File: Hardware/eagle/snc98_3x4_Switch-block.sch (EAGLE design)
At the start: 67 parts

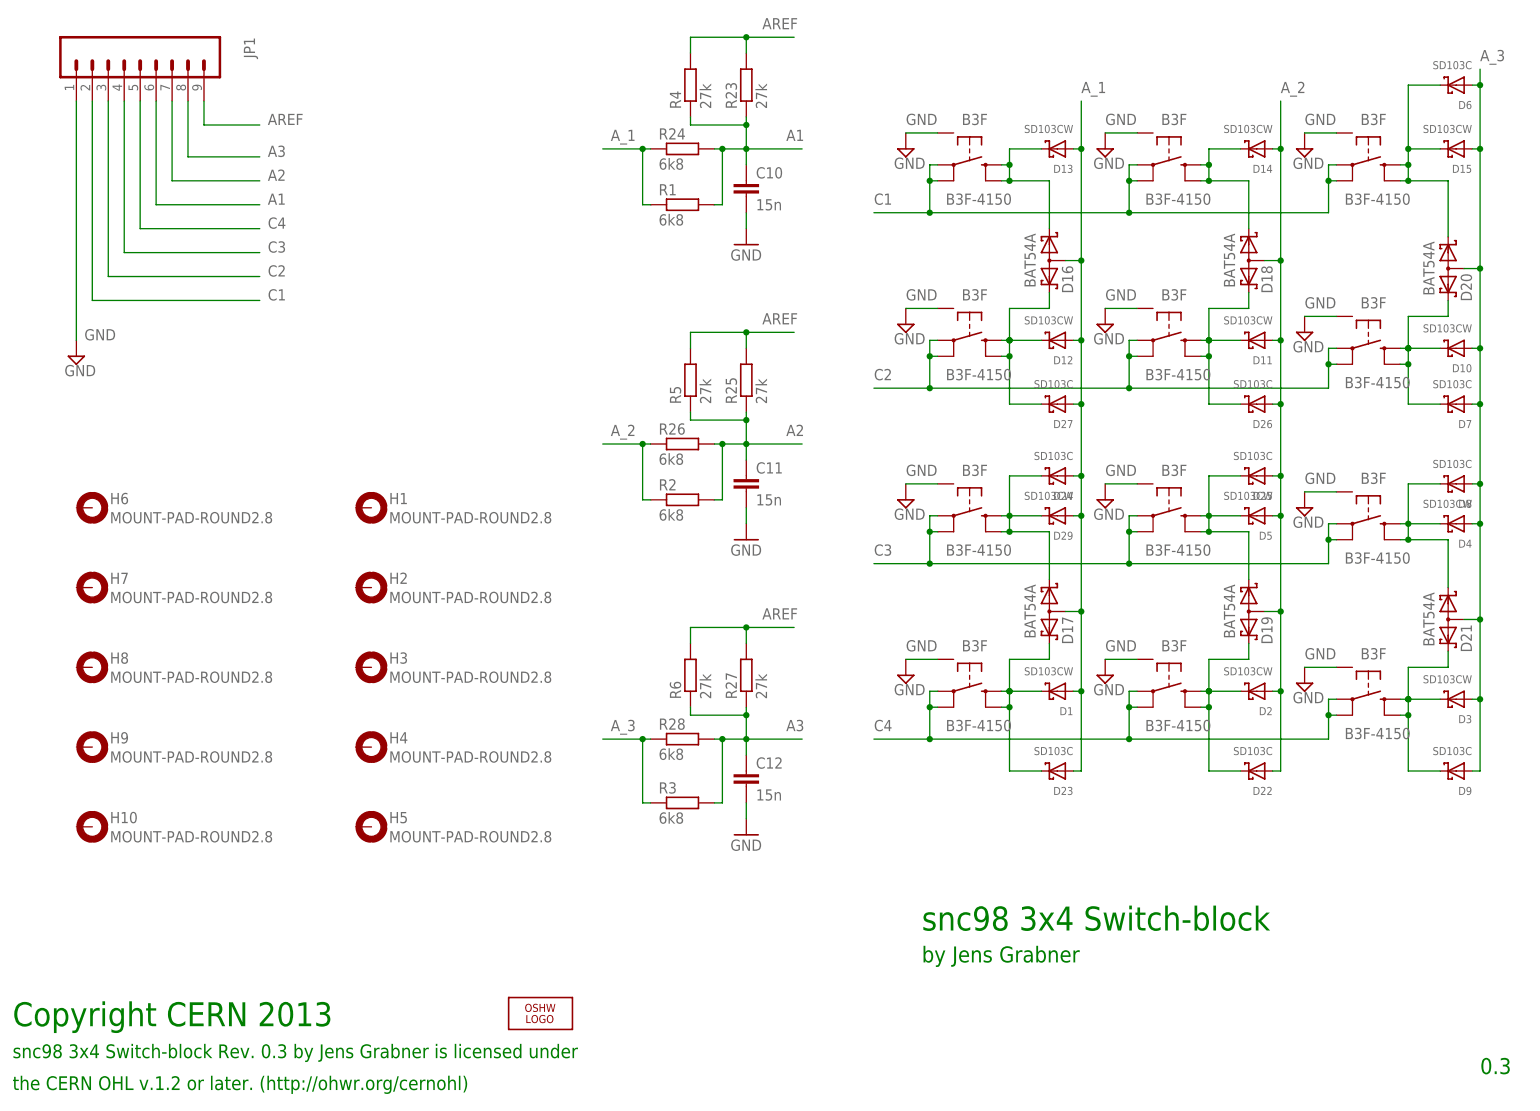
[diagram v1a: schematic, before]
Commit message: PCB cleaning V1.1
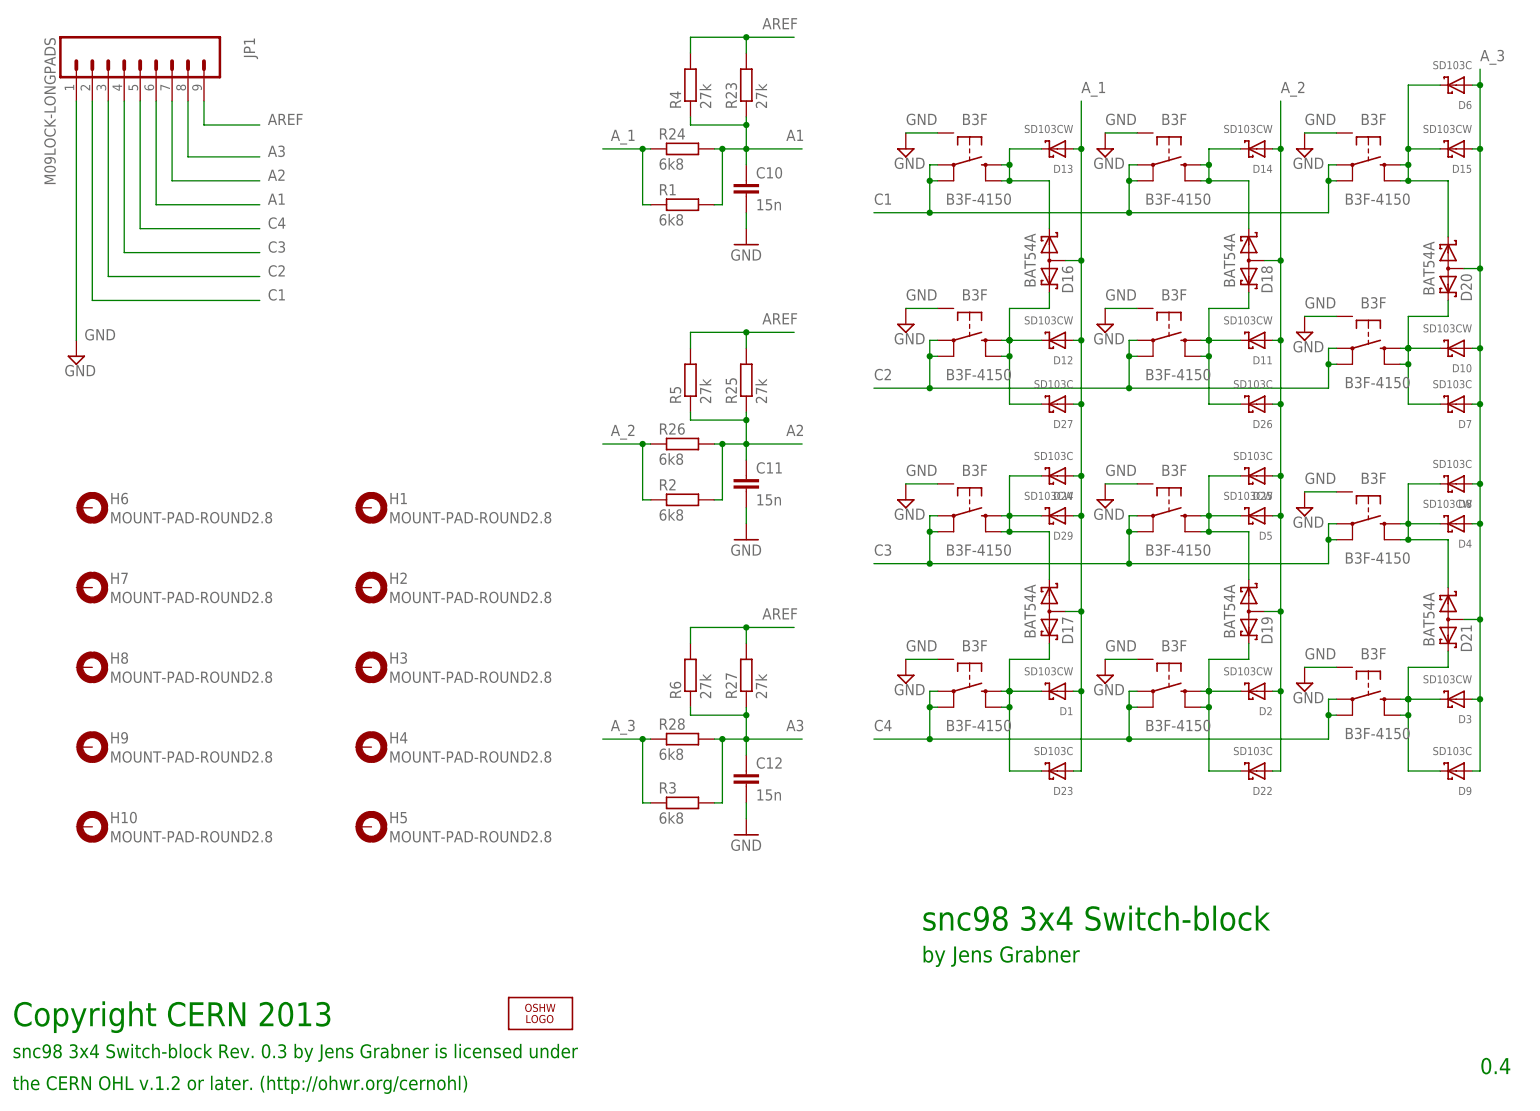
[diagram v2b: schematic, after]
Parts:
- JP1: value (none) -> M09LOCK-LONGPADS
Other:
- note added: "0.4"
- note removed: "0.3"
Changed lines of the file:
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@@
 <text x="149.86" y="30.48" size="3.81" layer="91" ratio="12">snc98 3x4 Switch-block</text>
 <text x="149.86" y="25.4" size="2.54" layer="91" ratio="12">by Jens Grabner</text>
-<text x="238.76" y="7.62" size="2.54" layer="91" ratio="12">0.3</text>
+<text x="238.76" y="7.62" size="2.54" layer="91" ratio="12">0.4</text>
 <text x="5.08" y="10.16" size="2.1844" layer="91" ratio="10">snc98 3x4 Switch-block Rev. 0.3 by Jens Grabner is licensed under</text>
 <text x="5.08" y="15.24" size="3.81" layer="91" ratio="12">Copyright CERN 2013</text>

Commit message: sinh()_cosh()_tanh() added
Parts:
- C10, C11, C12, D16, D17, D18, D19, D20, D21, H1, H4, H5, H6, H7, H8, JP1, LOGO1, R1, R2, R23, R24, R25, R26, R27, R28, R3, R4, R5, R6, S1, S10, S11, S12, S2, S3, S4, S5, S6, S7, S8, S9: OC_FARNELL (none) -> unknown
- D1, D10, D11, D12, D13, D14, D15, D2, D22, D23, D24, D25, D26, D27, D29, D3, D4, D5, D6, D7, D8, D9: MF (none) -> MULTICOMP; MPN (none) -> SD103CW-7-F; OC_FARNELL (none) -> 2306221
- H10, H2, H3, H9: value MOUNT-PAD-ROUND2.8 -> MOUNT-PAD-ROUND2.3; device holes:MOUNT-PAD-ROUND2.8 -> holes:MOUNT-PAD-ROUND2.3; OC_FARNELL (none) -> unknown

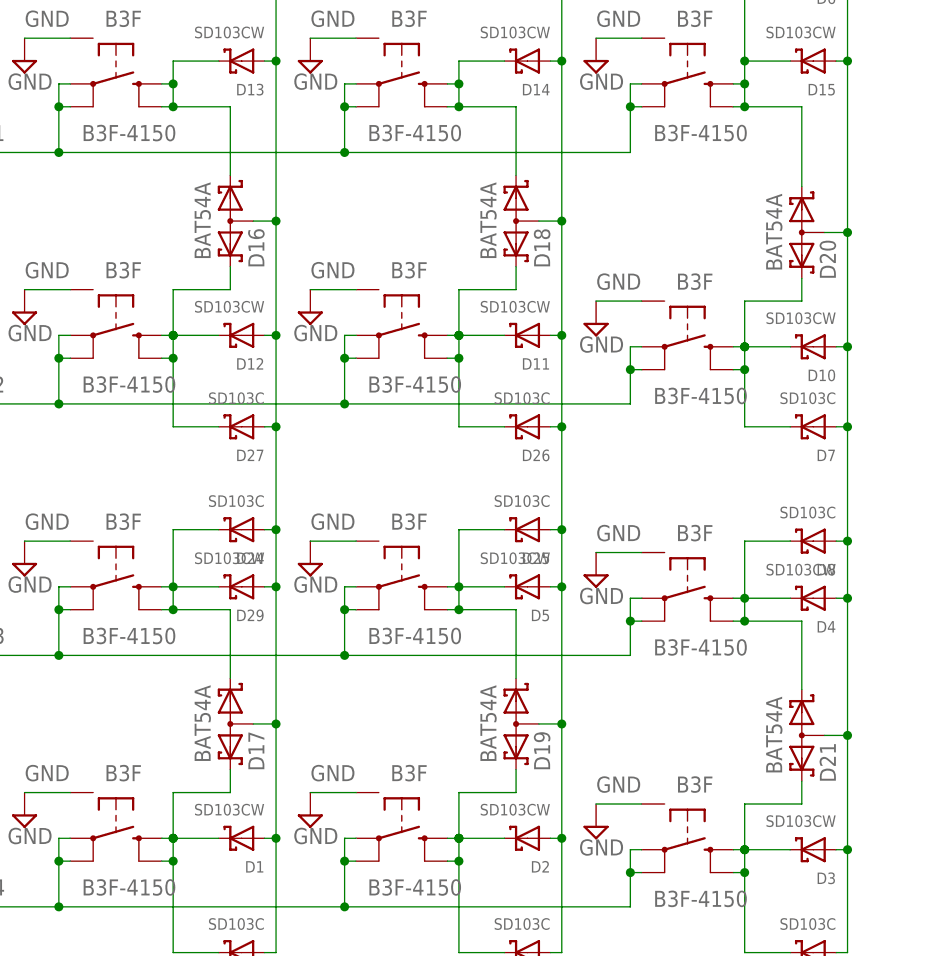
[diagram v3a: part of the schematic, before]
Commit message: PCB - add Tear Drop
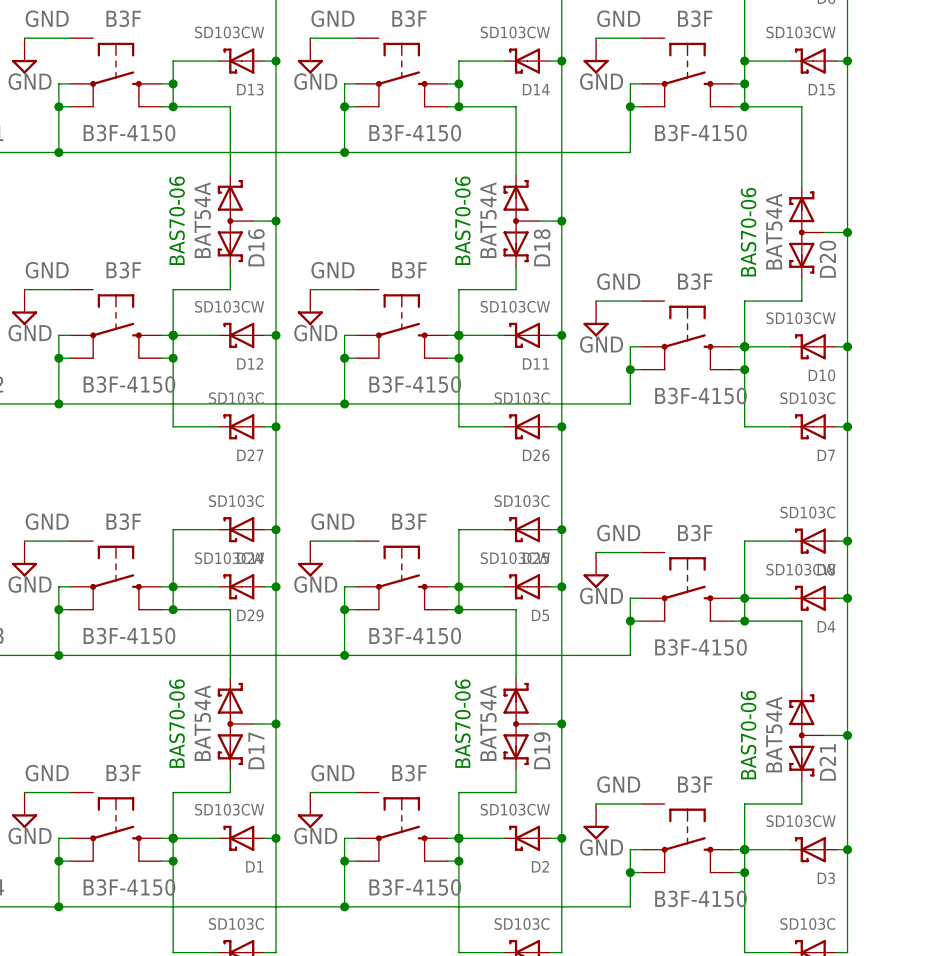
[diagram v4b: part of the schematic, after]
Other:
- note added: "BAS70-06"
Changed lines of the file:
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@@
 <setting verticaltext="up"/>
 </settings>
-<grid distance="0.1" unitdist="inch" unit="inch" style="lines" multiple="1" display="yes" altdistance="0.05" altunitdist="inch" altunit="inch"/>
+<grid distance="50" unitdist="mil" unit="mil" style="lines" multiple="1" display="yes" altdistance="0.05" altunitdist="inch" altunit="inch"/>
 <layers>
 <layer number="1" name="Top" color="4" fill="1" visible="no" active="no"/>
@@
 <text x="5.08" y="15.24" size="3.81" layer="91" ratio="12">Copyright CERN 2013</text>
 <text x="5.08" y="5.08" size="2.1844" layer="91" ratio="10">the CERN OHL v.1.2 or later. (http://ohwr.org/cernohl)</text>
+<text x="165.1" y="137.16" size="1.6764" layer="91" ratio="12" rot="R90" align="bottom-center">BAS70-06</text>
+<text x="196.85" y="137.16" size="1.6764" layer="91" ratio="12" rot="R90" align="bottom-center">BAS70-06</text>
+<text x="228.6" y="135.89" size="1.6764" layer="91" ratio="12" rot="R90" align="bottom-center">BAS70-06</text>
+<text x="228.6" y="80.01" size="1.6764" layer="91" ratio="12" rot="R90" align="bottom-center">BAS70-06</text>
+<text x="196.85" y="81.28" size="1.6764" layer="91" ratio="12" rot="R90" align="bottom-center">BAS70-06</text>
+<text x="165.1" y="81.28" size="1.6764" layer="91" ratio="12" rot="R90" align="bottom-center">BAS70-06</text>
 </plain>
 <instances>

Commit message: Gerber file added
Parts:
- added R10, R11, R9: 27k, rcl:R-EU_M0805
- added R33, R7, R8: 6k8, rcl:R-EU_M0805
- C10, C11, C12: TME_EU (none) -> CC0805KRX7R9153
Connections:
- net A1: now also R33.2, R9.1
- net A2: now also R10.1, R7.2
- net A3: now also R11.1, R8.2
- net AREF: now also R10.2, R11.2, R9.2
- net A_1: now also R33.1
- net A_2: now also R7.1
- net A_3: now also R8.1
